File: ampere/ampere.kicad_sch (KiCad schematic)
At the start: 17 parts, among them J1 USB_C_Receptacle_USB2.0_16P, U1 LP5907MFX-3.3, U2 STM32G474RETx, Y1 25 MHZ, Y2 32.768 KHZ

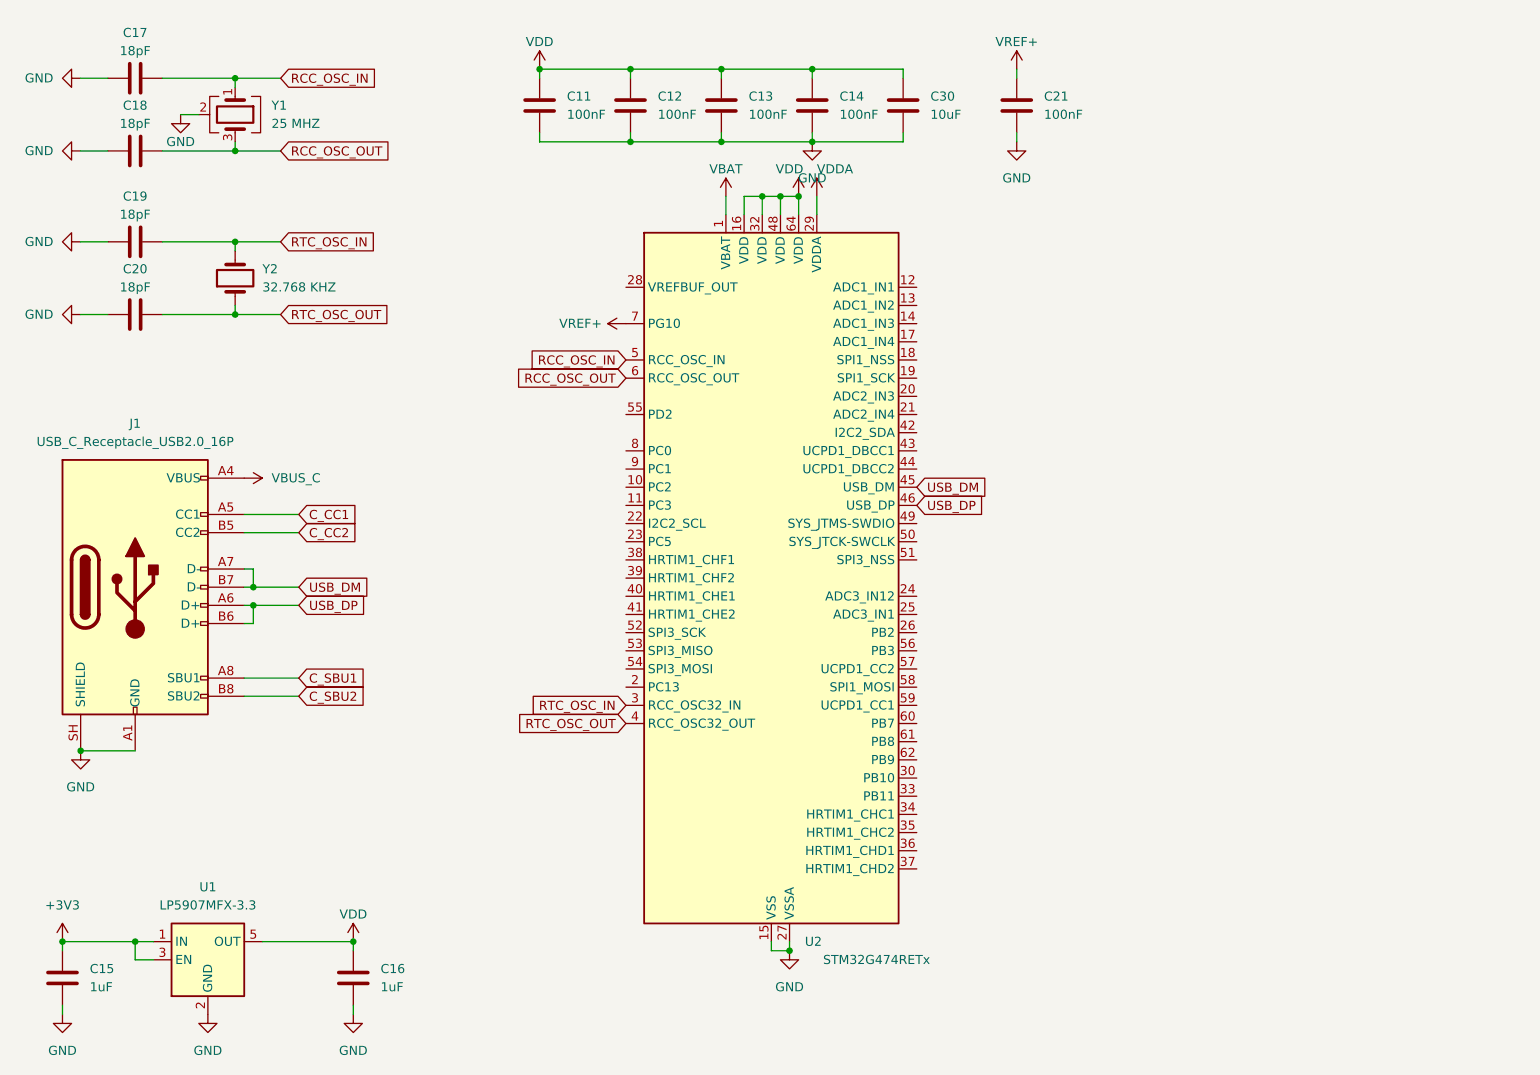
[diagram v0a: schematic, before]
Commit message: add LDOs, 90 percent of TPS55289s
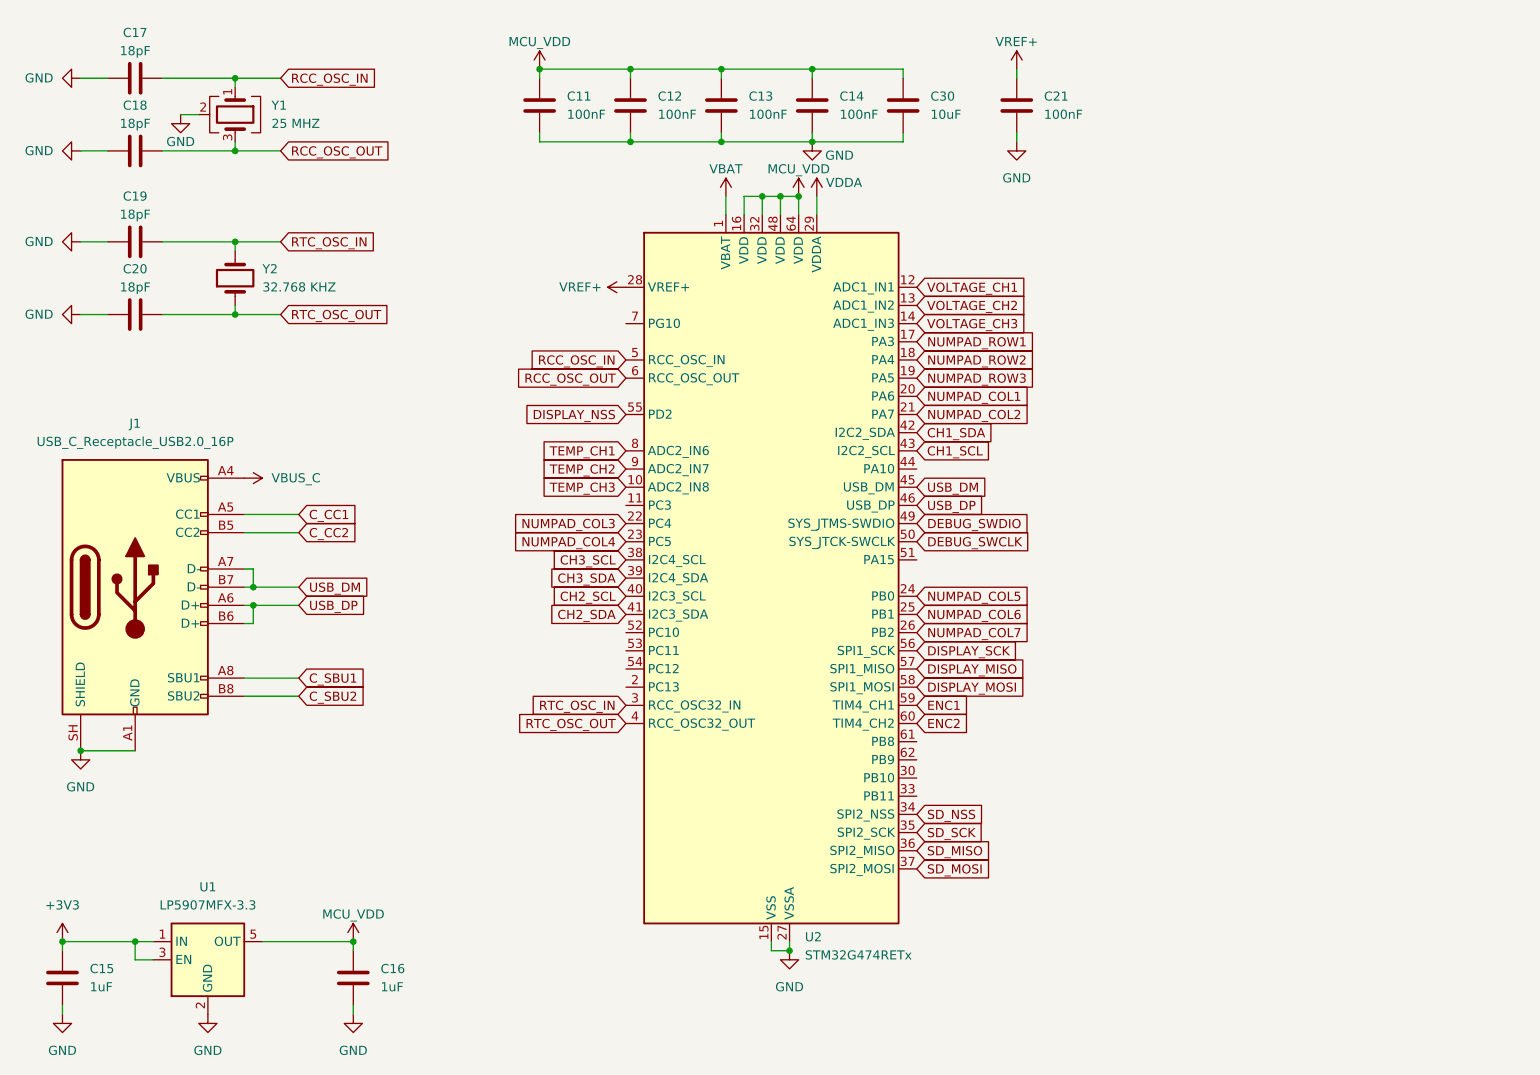
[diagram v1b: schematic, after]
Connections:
- net VREF+: now also U2.28 (VREF+); no longer U2.7 (PG10)
- net TEMP_CH3: now reaches U2.10 (PC2)
- net VOLTAGE_CH1: now reaches U2.12 (PA0)
- net VOLTAGE_CH2: now reaches U2.13 (PA1)
- net VOLTAGE_CH3: now reaches U2.14 (PA2)
- net NUMPAD_ROW1: now reaches U2.17 (PA3)
- net NUMPAD_ROW2: now reaches U2.18 (PA4)
- net NUMPAD_ROW3: now reaches U2.19 (PA5)
- net NUMPAD_COL1: now reaches U2.20 (PA6)
- net NUMPAD_COL2: now reaches U2.21 (PA7)
- net NUMPAD_COL3: now reaches U2.22 (PC4)
- net NUMPAD_COL4: now reaches U2.23 (PC5)
- net NUMPAD_COL5: now reaches U2.24 (PB0)
- net NUMPAD_COL6: now reaches U2.25 (PB1)
- net NUMPAD_COL7: now reaches U2.26 (PB2)
- net SD_NSS: now reaches U2.34 (PB12)
- net SD_SCK: now reaches U2.35 (PB13)
- net SD_MISO: now reaches U2.36 (PB14)
- net SD_MOSI: now reaches U2.37 (PB15)
- net CH3_SCL: now reaches U2.38 (PC6)
- net CH3_SDA: now reaches U2.39 (PC7)
- net CH2_SCL: now reaches U2.40 (PC8)
- net CH2_SDA: now reaches U2.41 (PC9)
- net CH1_SDA: now reaches U2.42 (PA8)
- net CH1_SCL: now reaches U2.43 (PA9)
- net DEBUG_SWDIO: now reaches U2.49 (PA13)
- net DEBUG_SWCLK: now reaches U2.50 (PA14)
- net DISPLAY_NSS: now reaches U2.55 (PD2)
- net DISPLAY_SCK: now reaches U2.56 (PB3)
- net DISPLAY_MISO: now reaches U2.57 (PB4)
- net DISPLAY_MOSI: now reaches U2.58 (PB5)
- net ENC1: now reaches U2.59 (PB6)
- net ENC2: now reaches U2.60 (PB7)
- net TEMP_CH1: now reaches U2.8 (PC0)
- net TEMP_CH2: now reaches U2.9 (PC1)
- net VDD renamed MCU_VDD

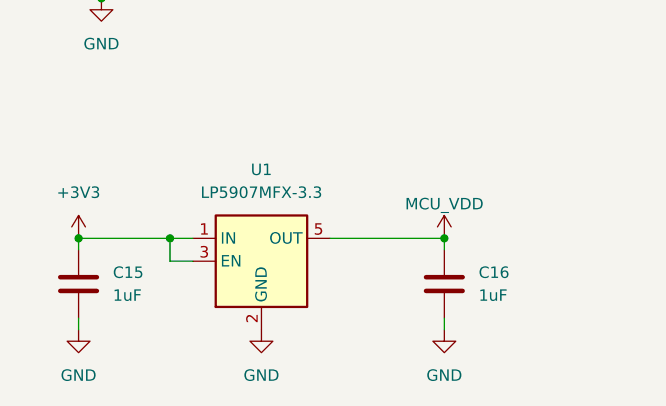
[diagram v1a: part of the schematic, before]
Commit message: add system power schematic
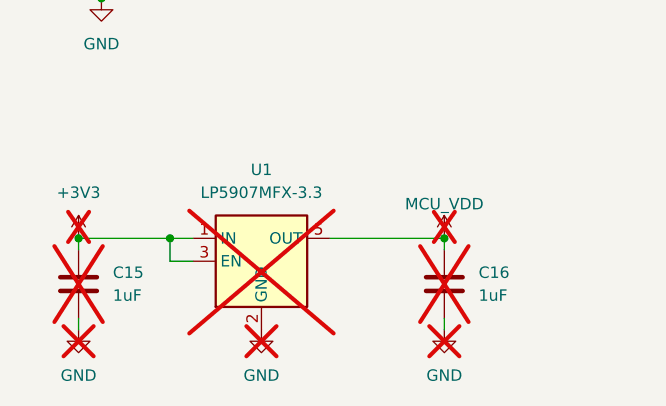
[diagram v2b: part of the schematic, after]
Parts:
- C15, C16, U1: now not fitted; now left out of the parts list
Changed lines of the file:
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@@
 		(body_style 1)
 		(exclude_from_sim no)
-		(in_bom yes)
-		(on_board yes)
-		(in_pos_files yes)
-		(dnp no)
+		(in_bom no)
+		(on_board yes)
+		(in_pos_files yes)
+		(dnp yes)
 		(fields_autoplaced yes)
 		(property "Reference" "#PWR03"
@@
 		(body_style 1)
 		(exclude_from_sim no)
-		(in_bom yes)
-		(on_board yes)
-		(in_pos_files yes)
-		(dnp no)
+		(in_bom no)
+		(on_board yes)
+		(in_pos_files yes)
+		(dnp yes)
 		(fields_autoplaced yes)
 		(property "Reference" "C16"
@@
 		(body_style 1)
 		(exclude_from_sim no)
-		(in_bom yes)
-		(on_board yes)
-		(in_pos_files yes)
-		(dnp no)
+		(in_bom no)
+		(on_board yes)
+		(in_pos_files yes)
+		(dnp yes)
 		(fields_autoplaced yes)
 		(property "Reference" "C15"
@@
 		(body_style 1)
 		(exclude_from_sim no)
-		(in_bom yes)
-		(on_board yes)
-		(in_pos_files yes)
-		(dnp no)
+		(in_bom no)
+		(on_board yes)
+		(in_pos_files yes)
+		(dnp yes)
 		(fields_autoplaced yes)
 		(property "Reference" "U1"
@@
 		(body_style 1)
 		(exclude_from_sim no)
-		(in_bom yes)
-		(on_board yes)
-		(in_pos_files yes)
-		(dnp no)
+		(in_bom no)
+		(on_board yes)
+		(in_pos_files yes)
+		(dnp yes)
 		(fields_autoplaced yes)
 		(property "Reference" "#PWR07"
@@
 		(body_style 1)
 		(exclude_from_sim no)
-		(in_bom yes)
-		(on_board yes)
-		(in_pos_files yes)
-		(dnp no)
+		(in_bom no)
+		(on_board yes)
+		(in_pos_files yes)
+		(dnp yes)
 		(fields_autoplaced yes)
 		(property "Reference" "#PWR08"
@@
 		(body_style 1)
 		(exclude_from_sim no)
-		(in_bom yes)
-		(on_board yes)
-		(in_pos_files yes)
-		(dnp no)
+		(in_bom no)
+		(on_board yes)
+		(in_pos_files yes)
+		(dnp yes)
 		(fields_autoplaced yes)
 		(property "Reference" "#PWR06"
@@
 		(body_style 1)
 		(exclude_from_sim no)
-		(in_bom yes)
-		(on_board yes)
-		(in_pos_files yes)
-		(dnp no)
+		(in_bom no)
+		(on_board yes)
+		(in_pos_files yes)
+		(dnp yes)
 		(property "Reference" "#PWR029"
 			(at 91.44 163.83 0)

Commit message: implement tps26750 and tpd4s480
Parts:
- removed C15, C16: 1uF, Capacitor_SMD:C_0402_1005Metric, symbol Device:C
- removed J1: USB_C_Receptacle_USB2.0_16P, Connector_USB:USB_C_Receptacle_JAE_DX07S016JA1R1500, symbol Connector:USB_C_Receptacle_USB2.0_16P
- removed U1: LP5907MFX-3.3, Package_TO_SOT_SMD:SOT-23-5, symbol Regulator_Linear:LP5907MFX-3.3
- added J1: USB_C_Receptacle, DX07S024JJ2R1300:JAE_DX07S024JJ2R1300, symbol Connector:USB_C_Receptacle
- added J5: Conn_02x13_Odd_Even, Connector_IDC:IDC-Header_2x13_P2.54mm_Horizontal, symbol Connector_Generic:Conn_02x13_Odd_Even
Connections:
- net C_CC1: now also J1.A5 (CC1)
- net C_CC2: now also J1.B5 (CC2)
- net C_SBU1: now also J1.A8 (SBU1)
- net C_SBU2: now also J1.B8 (SBU2)
- net GND: now also J1.A1 (GND), J1.A12 (GND), J1.B1 (GND), J1.B12 (GND), J1.SH (SHIELD)
- net USB_DM: now also J1.A7 (D-), J1.B7 (D-)
- net USB_DP: now also J1.A6 (D+), J1.B6 (D+)
- net VBUS_C: now also J1.A4 (VBUS), J1.A9 (VBUS), J1.B4 (VBUS), J1.B9 (VBUS)
- no-connect marks 0 -> 8

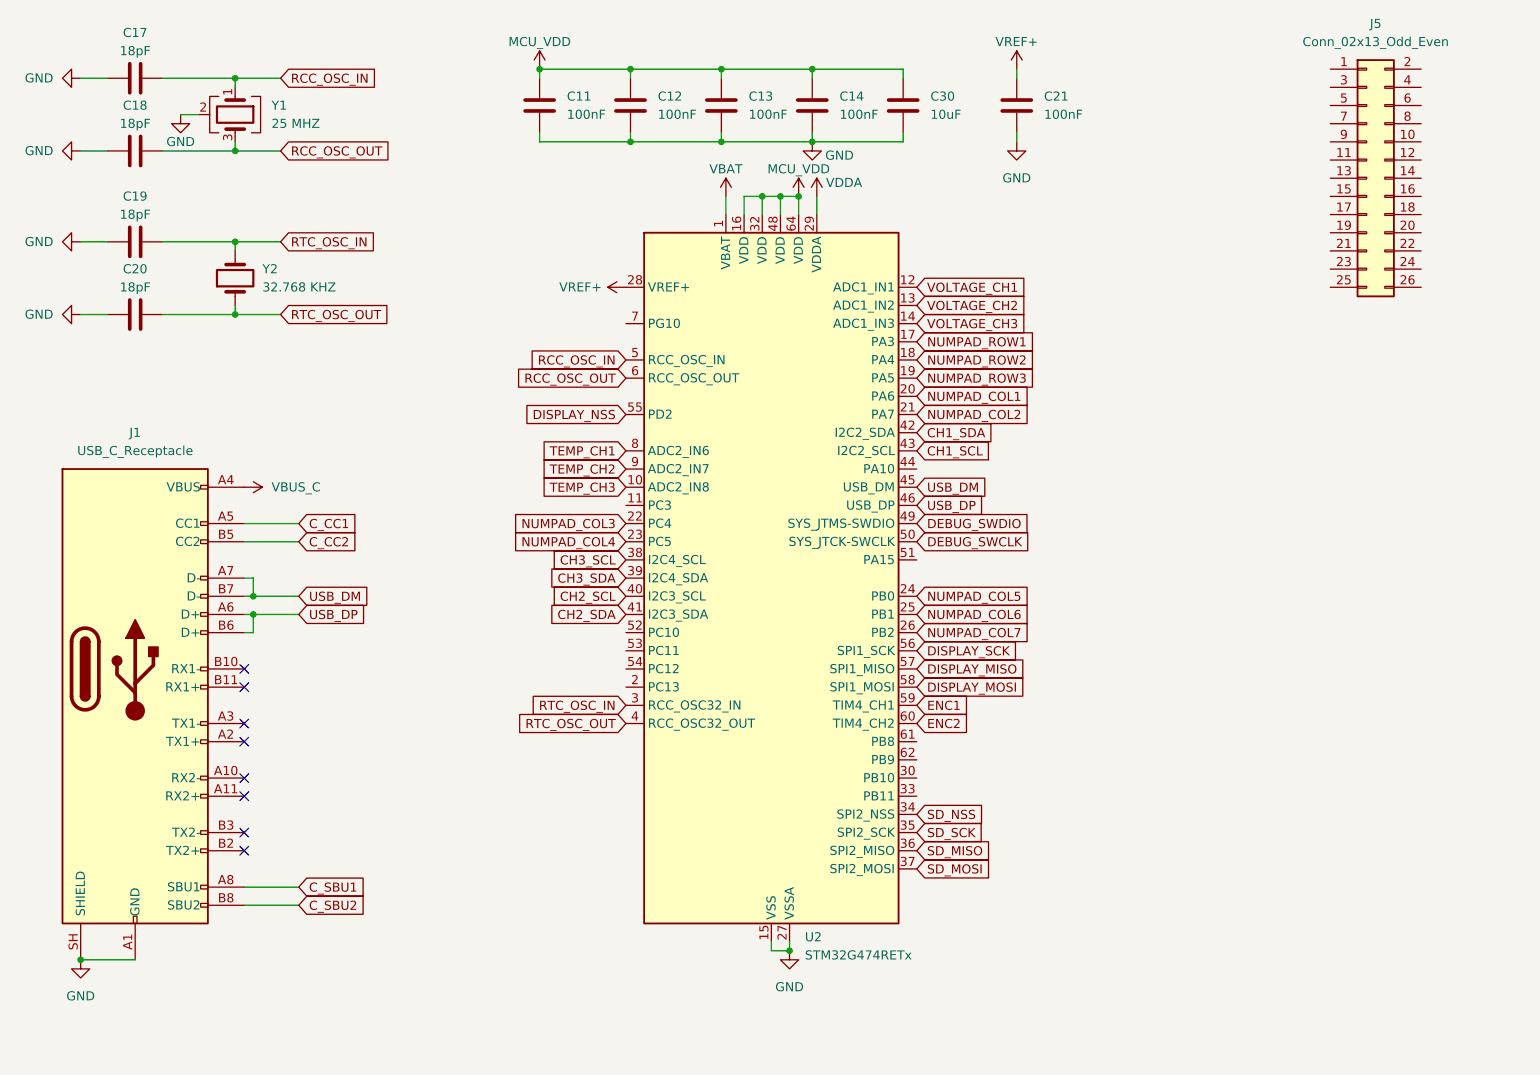
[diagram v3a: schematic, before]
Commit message: connect i2c up
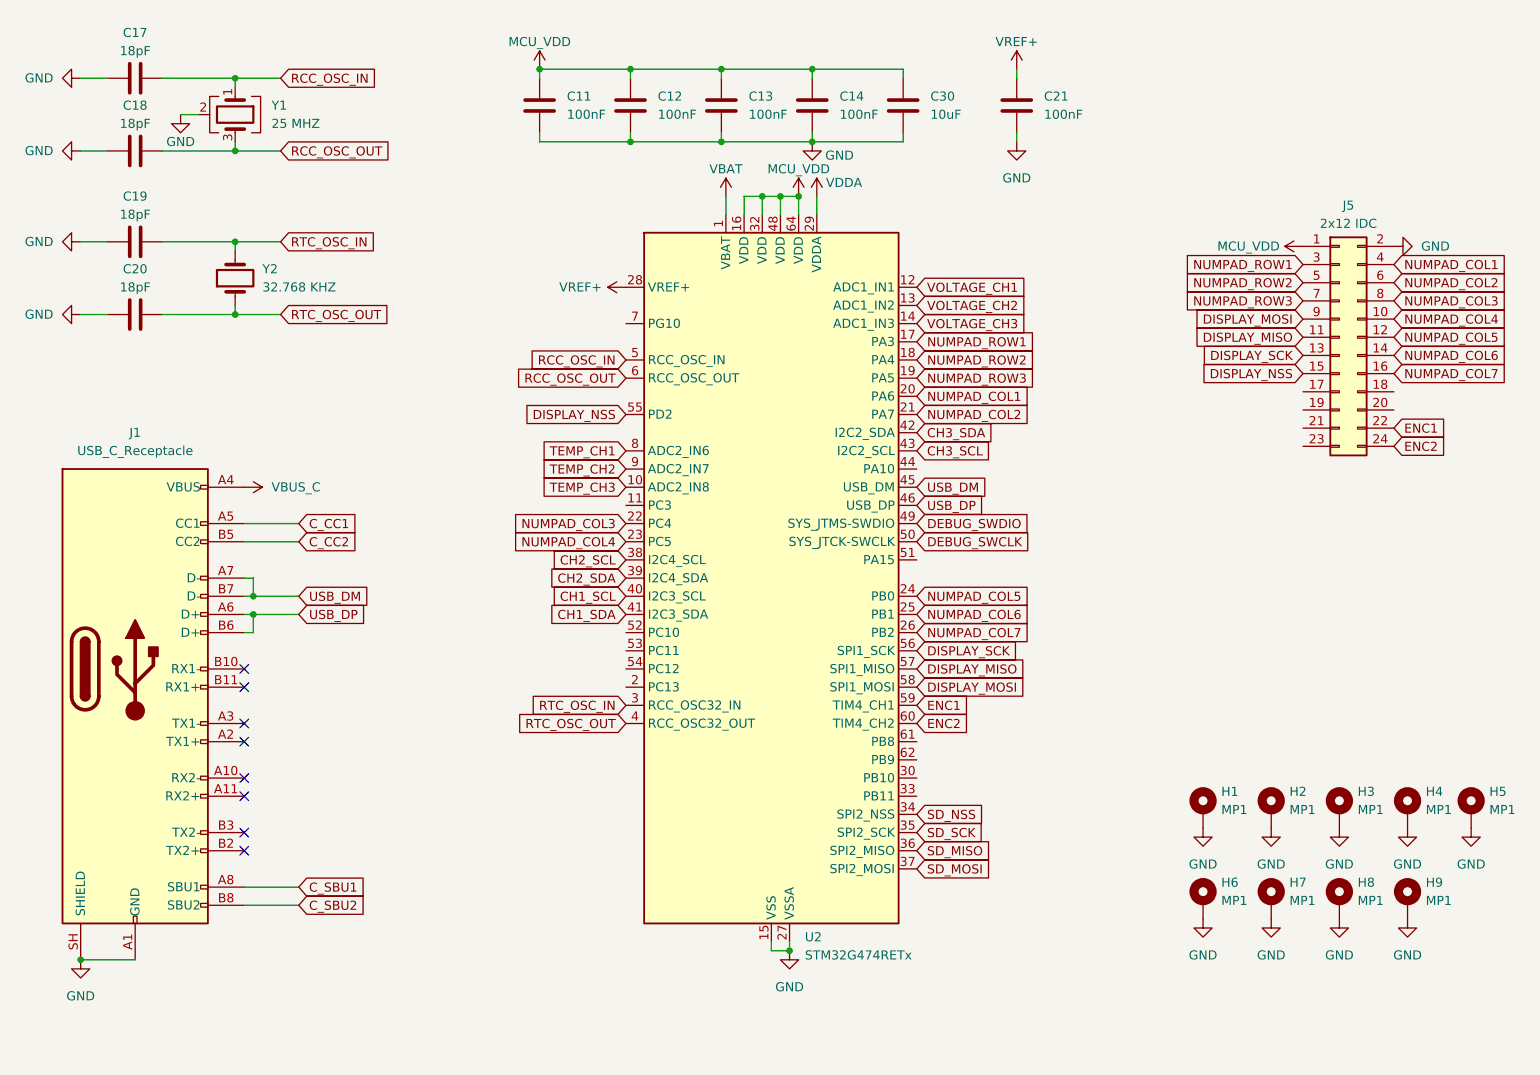
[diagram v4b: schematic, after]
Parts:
- removed J5: Conn_02x13_Odd_Even, Connector_IDC:IDC-Header_2x13_P2.54mm_Horizontal, symbol Connector_Generic:Conn_02x13_Odd_Even
- added H1, H2, H3, H4, H5: MP1, MountingHole:MountingHole_3.2mm_M3_DIN965, symbol Mechanical:MountingHole_Pad_MP
- added H6, H7, H8, H9: MP1, MountingHole:MountingHole_2.7mm_M2.5, symbol Mechanical:MountingHole_Pad_MP
- added J5: 2x12 IDC, Connector_IDC:IDC-Header_2x12_P2.54mm_Vertical, symbol Connector_Generic:Conn_02x12_Odd_Even
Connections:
- net CH1_SCL: now also U2.40 (PC8); no longer U2.43 (PA9)
- net CH1_SDA: now also U2.41 (PC9); no longer U2.42 (PA8)
- net CH2_SCL: now also U2.38 (PC6); no longer U2.40 (PC8)
- net CH2_SDA: now also U2.39 (PC7); no longer U2.41 (PC9)
- net CH3_SCL: now also U2.43 (PA9); no longer U2.38 (PC6)
- net CH3_SDA: now also U2.42 (PA8); no longer U2.39 (PC7)
- net DISPLAY_MISO: now also J5.11 (Pin_11)
- net DISPLAY_MOSI: now also J5.9 (Pin_9)
- net DISPLAY_NSS: now also J5.15 (Pin_15)
- net DISPLAY_SCK: now also J5.13 (Pin_13)
- net ENC1: now also J5.22 (Pin_22)
- net ENC2: now also J5.24 (Pin_24)
- net GND: now also H1.MP, H2.MP, H3.MP, H4.MP, H5.MP, H6.MP, H7.MP, H8.MP, H9.MP, J5.2 (Pin_2)
- net MCU_VDD: now also J5.1 (Pin_1)
- net NUMPAD_COL1: now also J5.4 (Pin_4)
- net NUMPAD_COL2: now also J5.6 (Pin_6)
- net NUMPAD_COL3: now also J5.8 (Pin_8)
- net NUMPAD_COL4: now also J5.10 (Pin_10)
- net NUMPAD_COL5: now also J5.12 (Pin_12)
- net NUMPAD_COL6: now also J5.14 (Pin_14)
- net NUMPAD_COL7: now also J5.16 (Pin_16)
- net NUMPAD_ROW1: now also J5.3 (Pin_3)
- net NUMPAD_ROW2: now also J5.5 (Pin_5)
- net NUMPAD_ROW3: now also J5.7 (Pin_7)
